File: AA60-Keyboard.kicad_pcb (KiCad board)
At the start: 2 copper layers, 191 parts, among them J2 USB_C_Receptacle_USB2.0_16P, SW1 SW_Push, SW10 MX_Keyswitch, SW100 MX_Keyswitch, SW101 MX_Keyswitch, SW11 MX_Keyswitch, SW12 MX_Keyswitch, SW13 MX_Keyswitch, SW14 MX_Keyswitch, SW15 MX_Keyswitch, SW16 MX_Keyswitch, SW17 MX_Keyswitch, SW18 MX_Keyswitch, SW19 MX_Keyswitch, SW2 SW_SPDT, SW20 MX_Keyswitch, SW21 MX_Keyswitch, SW22 MX_Keyswitch, SW23 MX_Keyswitch, SW24 MX_Keyswitch, SW25 MX_Keyswitch, SW26 MX_Keyswitch, SW27 MX_Keyswitch, SW28 MX_Keyswitch, SW29 MX_Keyswitch, SW3 MX_Keyswitch, SW30 MX_Keyswitch, SW31 MX_Keyswitch, SW32 MX_Keyswitch, SW33 MX_Keyswitch, SW34 MX_Keyswitch, SW35 MX_Keyswitch, SW36 MX_Keyswitch, SW37 MX_Keyswitch, SW38 MX_Keyswitch, SW39 MX_Keyswitch, SW4 MX_Keyswitch, SW40 MX_Keyswitch, SW41 MX_Keyswitch, SW42 MX_Keyswitch, SW43 MX_Keyswitch, SW44 MX_Keyswitch, SW45 MX_Keyswitch, SW46 MX_Keyswitch, SW47 MX_Keyswitch, SW48 MX_Keyswitch, SW49 MX_Keyswitch, SW5 MX_Keyswitch, SW50 MX_Keyswitch, SW51 MX_Keyswitch, SW52 MX_Keyswitch, SW53 MX_Keyswitch, SW54 MX_Keyswitch, SW55 MX_Keyswitch, SW56 MX_Keyswitch, SW57 MX_Keyswitch, SW58 MX_Keyswitch, SW59 MX_Keyswitch, SW6 MX_Keyswitch, SW60 MX_Keyswitch, SW61 MX_Keyswitch, SW62 MX_Keyswitch, SW63 MX_Keyswitch, SW64 MX_Keyswitch, SW65 MX_Keyswitch, SW66 MX_Keyswitch, SW67 MX_Keyswitch, SW68 MX_Keyswitch, SW69 MX_Keyswitch, SW7 MX_Keyswitch, SW70 MX_Keyswitch, SW71 MX_Keyswitch, SW72 MX_Keyswitch, SW73 MX_Keyswitch, SW75 MX_Keyswitch, SW76 MX_Keyswitch, SW77 MX_Keyswitch, SW78 MX_Keyswitch, SW79 MX_Keyswitch, SW8 MX_Keyswitch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

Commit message: Putting diodes in their place
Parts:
- moved D33 402.6 mm to (36.5, 28.2), turned to -90 degrees
- moved D18 395.1 mm to (31.2, 24.1), turned to -90 degrees
- moved D34 374.4 mm to (41.8, 32.5), turned to -90 degrees
- moved D17 374.2 mm to (41.8, 39.2), turned to -90 degrees
- moved D4 371.2 mm to (51.3, 23.9), turned to -90 degrees
- moved D1 371.0 mm to (31.2, 30.9), turned to -90 degrees
- moved D3 369.4 mm to (36.5, 35.0), turned to -90 degrees
- moved D2 368.5 mm to (47.0, 24.1), turned to -90 degrees
- moved R3 225.8 mm to (198.9, 29.3), turned to -90 degrees
- moved R2 220.7 mm to (203.4, 29.3), turned to 90 degrees
- moved U2 220.3 mm to (201.3, 33.6)
- moved F1 217.9 mm to (207.2, 29.4), turned to -90 degrees
- moved SW1 208.1 mm to (238.2, 28.1)
- moved R1 201.6 mm to (220.5, 37.2), turned to 90 degrees
- moved SW2 200.6 mm to (215.7, 34.4), turned to -90 degrees
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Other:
- board outline added: 349.2 x 151.6 mm

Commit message: Putting diodes in their place
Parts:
- C1, C2, C3, C4, C5, C6, C7, D1, D10, D11, D12, D13, D14, D15, D16, D17, D18, D19, D2, D20, D21, D22, D23, D24, D25, D26, D27, D28, D29, D3, D30, D31, D32, D33, D34, D35, D36, D37, D38, D39, D4, D40, D41, D42, D43, D44, D45, D46, D47, D48, D49, D5, D50, D51, D52, D53, D54, D55, D56, D57, D58, D59, D6, D60, D61, D62, D63, D64, D65, D66, D67, D68, D69, D7, D70, D71, D73, D74, D75, D76, D77, D79, D8, D80, D81, D85, D86, D87, D9, D91, D92, D93, D98, D99, F1, J2, R1, R2, R3, SW1, SW2, U1, U2, U3: moved to B.Cu
- SW10, SW100, SW101, SW11, SW12, SW13, SW14, SW15, SW16, SW17, SW18, SW21, SW22, SW23, SW24, SW25, SW26, SW27, SW28, SW29, SW3, SW30, SW31, SW32, SW33, SW34, SW37, SW39, SW4, SW41, SW43, SW45, SW47, SW49, SW5, SW51, SW52, SW53, SW54, SW55, SW56, SW57, SW58, SW59, SW6, SW60, SW61, SW62, SW63, SW64, SW65, SW66, SW67, SW68, SW69, SW7, SW70, SW71, SW72, SW75, SW76, SW77, SW79, SW8, SW81, SW87, SW88, SW89, SW9, SW93, SW94, SW95: footprint MX_Hotswap:MX-Hotswap-1U -> MX_Solderable:MX-Solderable-1U
- SW19, SW83: footprint MX_Hotswap:MX-Hotswap-1.5U -> MX_Solderable:MX-Solderable-1.5U
- SW20: footprint MX_Hotswap:MX-Hotswap-1.75U -> MX_Solderable:MX-Solderable-1.75U
- SW35, SW78: footprint MX_Hotswap:MX-Hotswap-2.25U -> MX_Solderable:MX-Solderable-2.25U
- SW36, SW38, SW40, SW44, SW46, SW48, SW50: footprint MX_Hotswap:MX-Hotswap-1.25U -> MX_Solderable:MX-Solderable-1.25U
- SW42: footprint MX_Hotswap:MX-Hotswap-6.25U -> MX_Solderable:MX-Solderable-6.25U
- SW73: footprint MX_Hotswap:MX-Hotswap-2.75U -> MX_Solderable:MX-Solderable-2.75U
- SW82: footprint MX_Hotswap:MX-Hotswap-2U -> MX_Solderable:MX-Solderable-2U
- moved D5 316.8 mm to (96.3, 61.7), turned to 90 degrees
- moved D19 312.1 mm to (67.7, 106.2), turned to 90 degrees
- moved D7 311.9 mm to (115.3, 61.7), turned to 90 degrees
- moved D6 311.0 mm to (77.2, 87.1), turned to 90 degrees
- moved D9 308.3 mm to (134.3, 61.7), turned to 90 degrees
- moved D8 304.4 mm to (96.3, 87.1), turned to 90 degrees
- moved D21 304.3 mm to (86.7, 106.2), turned to 90 degrees
- moved D11 302.2 mm to (162.9, 61.7), turned to 90 degrees
- moved D10 298.9 mm to (115.3, 87.1), turned to 90 degrees
- moved D20 297.6 mm to (72.4, 125.2), turned to 90 degrees
- moved D22 289.3 mm to (91.5, 125.2), turned to 90 degrees
- moved D55 284.2 mm to (248.7, 61.7), turned to 90 degrees
- moved D36 275.5 mm to (65.3, 163.3), turned to 90 degrees
- moved D23 272.9 mm to (105.8, 106.2), turned to 90 degrees
- moved D49 271.7 mm to (220.1, 61.7), turned to 90 degrees
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
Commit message: PCB matrix front and back traces
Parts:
- moved D91 220.3 mm to (369.3, 61.7)
- moved D98 214.8 mm to (369.3, 87.1)
- moved D99 209.0 mm to (369.3, 106.2)
- moved D79 207.5 mm to (331.2, 61.7)
- moved D85 197.9 mm to (350.2, 61.7)
- moved D66 197.5 mm to (369.3, 163.3)
- moved D92 192.8 mm to (350.2, 87.1)
- moved D93 185.9 mm to (350.2, 106.2)
- moved D77 179.4 mm to (350.2, 144.3)
- moved D73 178.3 mm to (305.8, 61.7)
- moved D86 169.4 mm to (331.2, 87.1)
- moved D61 162.1 mm to (267.7, 61.7)
- moved D87 160.9 mm to (331.2, 106.2)
- moved D67 158.1 mm to (286.8, 61.7)
- moved D80 137.5 mm to (296.3, 87.1)
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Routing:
- net ROW5: track 0.00 -> 465.1 mm
- net ROW4: track 0.00 -> 435.2 mm
- net ROW3: track 0.00 -> 409.6 mm
- net ROW2: track 0.00 -> 400.7 mm
- net ROW1: track 0.00 -> 386.5 mm
- net ROW0: track 0.00 -> 360.6 mm
- net COL10: track 0.00 -> 253.4 mm
- net COL9: track 0.00 -> 247.8 mm
- net COL8: track 0.00 -> 242.0 mm
- net COL7: track 0.00 -> 235.1 mm
- net COL6: track 0.00 -> 233.8 mm
- net COL5: track 0.00 -> 224.7 mm
- net COL4: track 0.00 -> 206.9 mm
- net COL12: track 0.00 -> 174.6 mm
- net COL3: track 0.00 -> 161.5 mm
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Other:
- board size 349.2 x 151.6 mm -> 355.6 x 154.8 mm

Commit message: Microcontroller Circuitry
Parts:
- moved C2 80.8 mm to (223.1, 28.6), turned to 0 degrees
- moved C5 77.6 mm to (241.4, 23.7), turned to 90 degrees
- moved C7 77.5 mm to (234.1, 21.1), turned to 90 degrees
- moved C4 77.1 mm to (219.2, 28.6), turned to 180 degrees
- moved SW1 76.3 mm to (238.6, 22.4), turned to 90 degrees
- moved C1 75.5 mm to (223.1, 26.5), turned to 0 degrees
- moved C3 71.9 mm to (219.2, 26.5), turned to 180 degrees
- moved C6 62.3 mm to (225.1, 22.1)
- moved U1 50.0 mm to (222.2, 36.2), turned to -90 degrees
- moved U3 38.3 mm to (197.2, 41.0), turned to 180 degrees
- moved R1 34.3 mm to (214.4, 39.5), turned to -90 degrees
- moved SW2 31.7 mm to (213.7, 20.8), turned to 0 degrees
- moved R3 4.68 mm to (206.2, 27.8), turned to 0 degrees
- moved U2 3.19 mm to (197.3, 36.0)
- moved F1 2.48 mm to (196.0, 29.3)
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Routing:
- net GND: track 0.00 -> 74.9 mm
- net +5V: track 0.00 -> 41.2 mm, vias 0 -> 2
- net USB_DM: track 0.00 -> 34.0 mm
- net USB_DP: track 0.00 -> 33.4 mm
- net +3.3V: track 0.00 -> 26.5 mm
- net nRST: track 0.00 -> 21.0 mm
- net Net-(SW2-B): track 0.00 -> 16.4 mm
- net VBUS: track 0.00 -> 10.4 mm
- net Net-(D18-A): track 0.00 -> 9.35 mm
- net Net-(D70-A): track 0.00 -> 9.34 mm
- net Net-(D21-A): track 0.00 -> 9.34 mm
- net Net-(J2-CC2): track 0.00 -> 6.88 mm
- net BOOT0: track 0.00 -> 5.11 mm
- net Net-(J2-CC1): track 0.00 -> 4.87 mm
- net Net-(D85-A): track 9.58 -> 9.74 mm, vias 1 -> 0
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
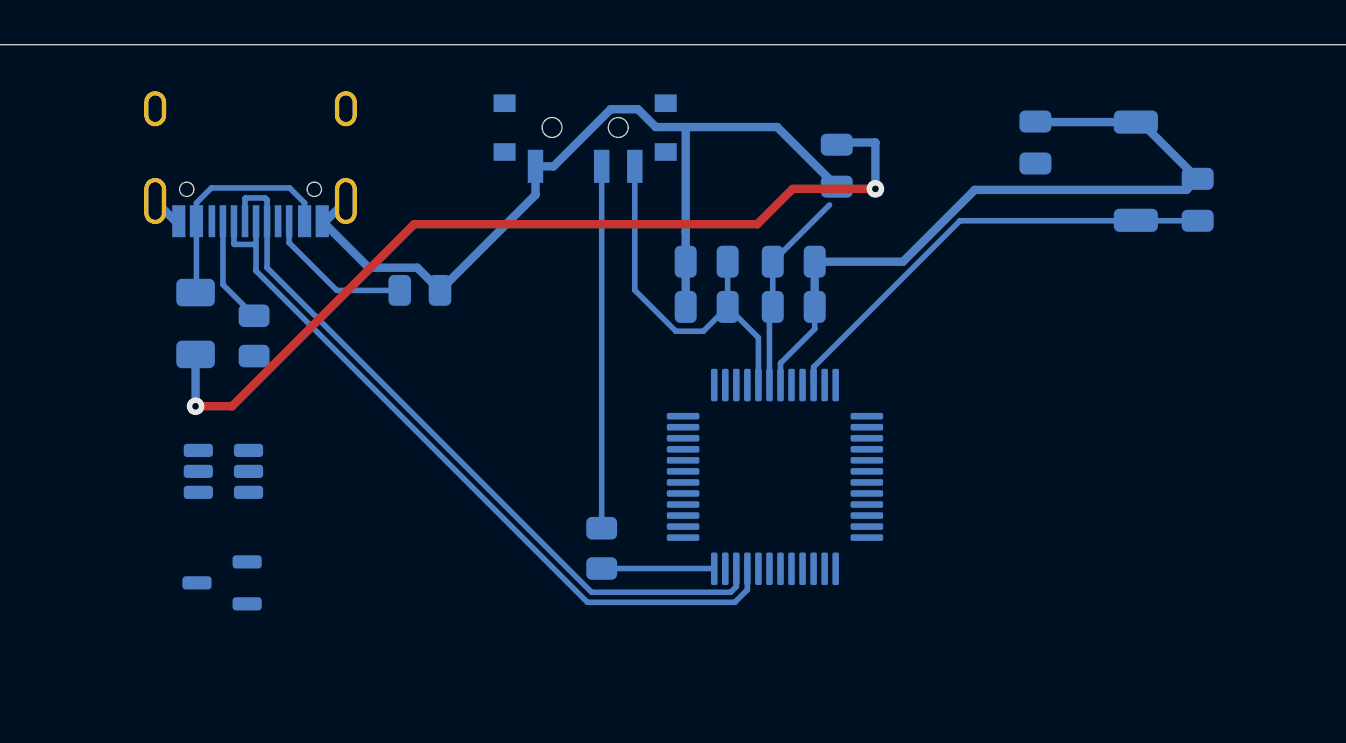
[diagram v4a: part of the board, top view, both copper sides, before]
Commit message: USB and microcontroller circuits wired (is ESD for CC lines needed??)
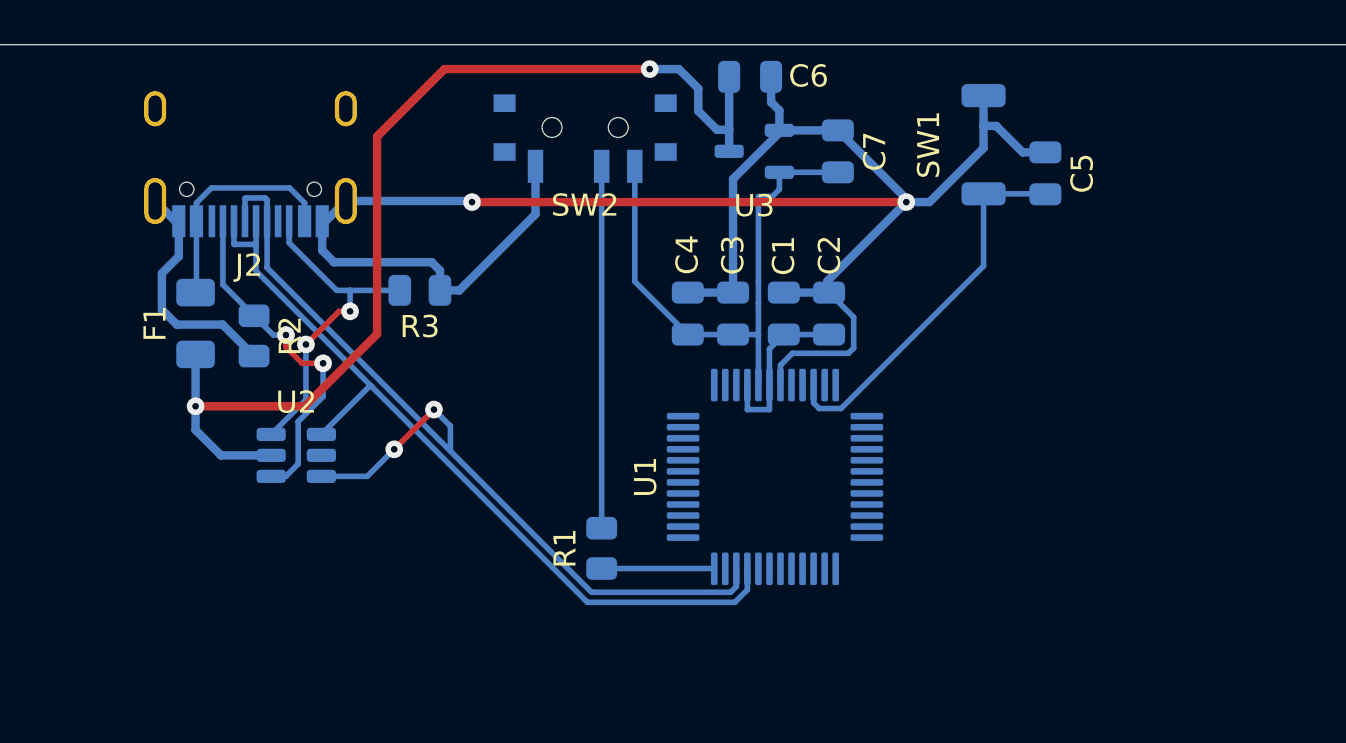
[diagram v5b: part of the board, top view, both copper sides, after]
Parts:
- moved U3 31.0 mm to (221.3, 21.5)
- moved C7 8.96 mm to (225.1, 21.5)
- moved C5 7.00 mm to (234.5, 22.5)
- moved SW1 7.00 mm to (231.7, 21.2)
- moved C6 5.62 mm to (221.1, 18.1), turned to 0 degrees
- moved U2 3.38 mm to (200.6, 35.3)
- moved C3 2.64 mm to (220.3, 28.9), turned to 90 degrees
- moved C1 2.39 mm to (222.7, 28.9), turned to 90 degrees
- moved C2 1.63 mm to (224.7, 28.9), turned to 90 degrees
- moved C4 0.91 mm to (218.3, 28.9), turned to 90 degrees
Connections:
- J2 pad A5: Net-(J2-CC1) -> /CC1
- J2 pad B5: Net-(J2-CC2) -> /CC2
- R2 pad 2: Net-(J2-CC1) -> /CC1
- R3 pad 1: Net-(J2-CC2) -> /CC2
- U2 pad 1: unconnected-(U2-IO1-Pad1) -> USB_DM
- U2 pad 3: unconnected-(U2-IO2-Pad3) -> USB_DP
- U2 pad 4: unconnected-(U2-IO3-Pad4) -> /CC1
- U2 pad 6: unconnected-(U2-IO4-Pad6) -> /CC2
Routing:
- net GND: track 74.9 -> 99.0 mm, vias 0 -> 2
- net /CC1: track 0.00 -> 15.7 mm, vias 0 -> 2
- net /CC2: track 0.00 -> 15.2 mm, vias 0 -> 2
- net USB_DP: track 33.4 -> 42.0 mm, vias 0 -> 2
- net +5V: track 41.2 -> 48.2 mm
- net Net-(J2-CC2): track 6.88 -> 0.00 mm
- net +3.3V: track 26.5 -> 32.7 mm
- net Net-(J2-CC1): track 4.87 -> 0.00 mm
- net nRST: track 21.0 -> 17.4 mm
- net USB_DM: track 34.0 -> 37.1 mm

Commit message: Microcontroller Matrix Routed
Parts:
- moved R1 14.4 mm to (214.3, 25.1)
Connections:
- U1 pad 13: unconnected-(U1-PA2-Pad13) -> ROW5
- U1 pad 14: unconnected-(U1-PA3-Pad14) -> ROW4
- U1 pad 15: unconnected-(U1-PA4-Pad15) -> ROW3
- U1 pad 16: unconnected-(U1-PA5-Pad16) -> ROW2
- U1 pad 17: unconnected-(U1-PA6-Pad17) -> ROW1
- U1 pad 18: unconnected-(U1-PA7-Pad18) -> ROW0
- U1 pad 29: unconnected-(U1-PA9/UCPD1_DBCC1-Pad29) -> COL15
- U1 pad 30: unconnected-(U1-PC6-Pad30) -> COL14
- U1 pad 31: unconnected-(U1-PC7-Pad31) -> COL13
- U1 pad 32: unconnected-(U1-PA10/UCPD1_DBCC2-Pad32) -> COL12
- U1 pad 37: unconnected-(U1-PA15-Pad37) -> COL9
- U1 pad 38: unconnected-(U1-PD0-Pad38) -> COL10
- U1 pad 39: unconnected-(U1-PD1-Pad39) -> COL11
- U1 pad 40: unconnected-(U1-PD2-Pad40) -> COL8
- U1 pad 41: unconnected-(U1-PD3-Pad41) -> COL7
- U1 pad 42: unconnected-(U1-PB3-Pad42) -> COL6
- U1 pad 43: unconnected-(U1-PB4-Pad43) -> COL5
- U1 pad 44: unconnected-(U1-PB5-Pad44) -> COL4
- U1 pad 45: unconnected-(U1-PB6-Pad45) -> COL3
- U1 pad 46: unconnected-(U1-PB7-Pad46) -> COL2
- U1 pad 47: unconnected-(U1-PB8-Pad47) -> COL1
- U1 pad 48: unconnected-(U1-PB9-Pad48) -> COL0
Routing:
- net COL0: track 110.5 -> 315.6 mm, vias 0 -> 1
- net COL1: track 133.2 -> 299.0 mm, vias 0 -> 1
- net COL2: track 128.9 -> 274.9 mm, vias 0 -> 1
- net COL15: track 57.0 -> 200.2 mm, vias 0 -> 1
- net ROW5: track 465.1 -> 608.3 mm
- net ROW4: track 435.2 -> 577.6 mm
- net ROW3: track 409.6 -> 551.3 mm
- net ROW2: track 400.7 -> 541.6 mm
- net ROW1: track 386.5 -> 526.6 mm
- net ROW0: track 360.6 -> 500.0 mm
- net COL3: track 161.5 -> 288.6 mm, vias 0 -> 1
- net COL14: track 57.0 -> 182.0 mm, vias 0 -> 1
- net COL4: track 206.9 -> 314.0 mm, vias 0 -> 1
- net COL13: track 74.8 -> 181.6 mm, vias 0 -> 1
- net COL11: track 136.3 -> 223.1 mm, vias 0 -> 1
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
